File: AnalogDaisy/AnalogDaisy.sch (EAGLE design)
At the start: 21 parts, among them J1 1X2-3.5MM, J2 1X2-3.5MM, J3 1X2-3.5MM, J4 1X2-3.5MM, J5 1X2-3.5MM, J7 POWER_JACKPTH_BREAD, Q1 35A/25V/8.5mΩ, Q3 35A/25V/8.5mΩ, Q5 35A/25V/8.5mΩ, Q6 35A/25V/8.5mΩ

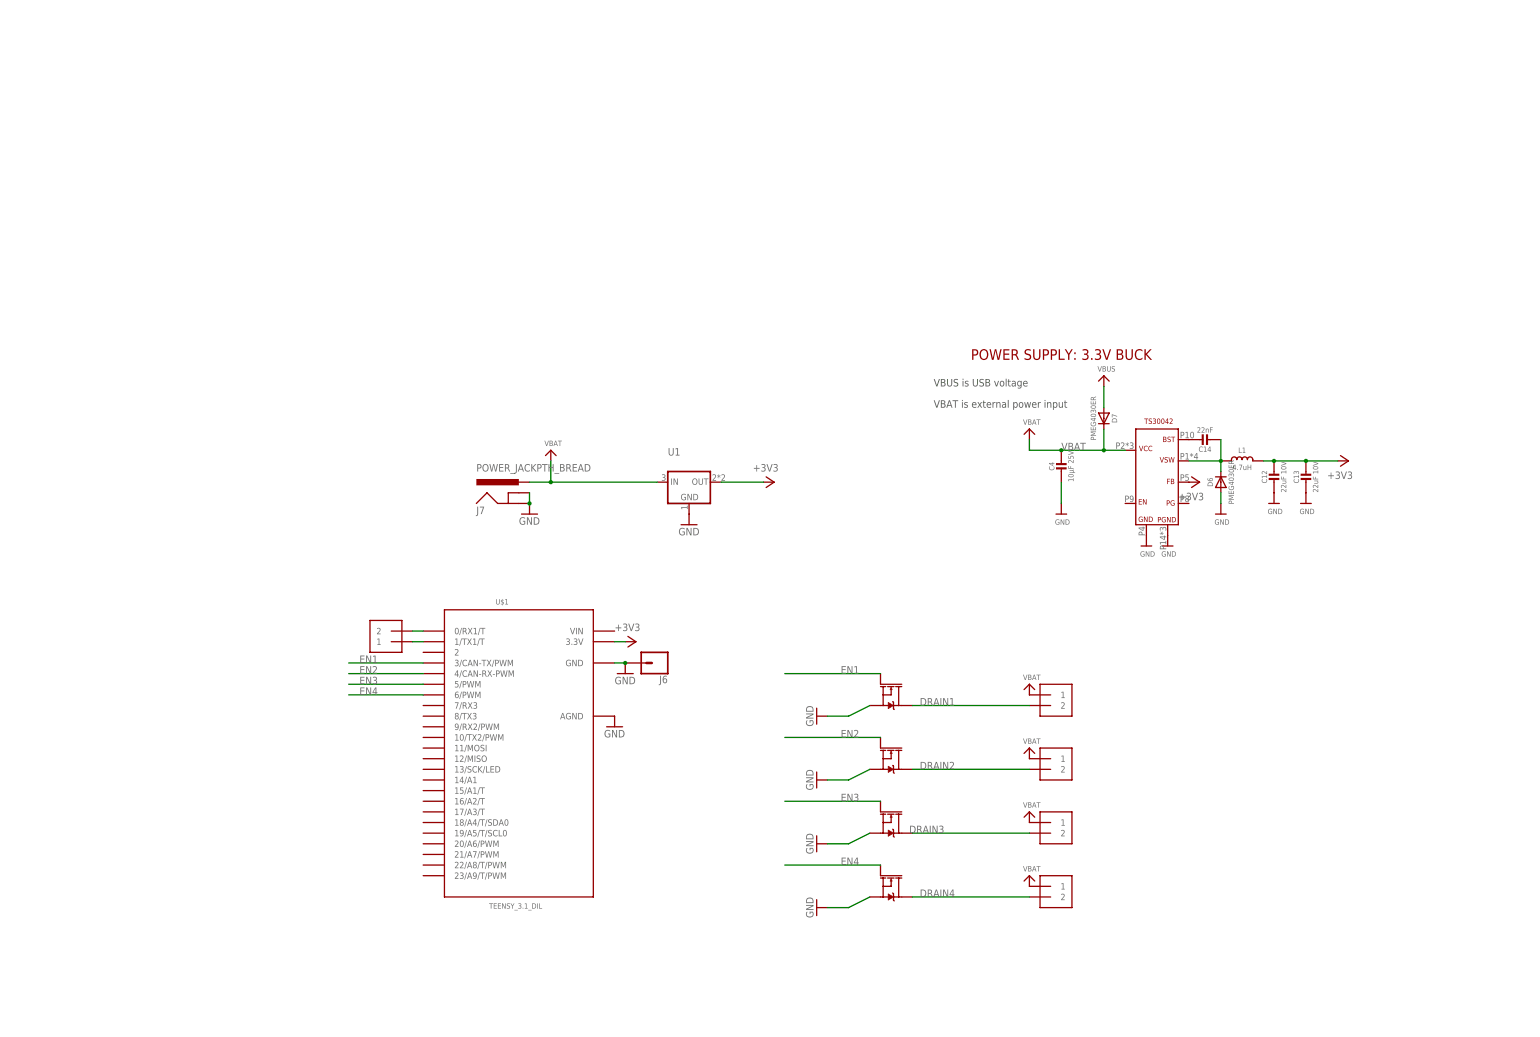
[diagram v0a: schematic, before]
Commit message: Updated AnalogDaisy
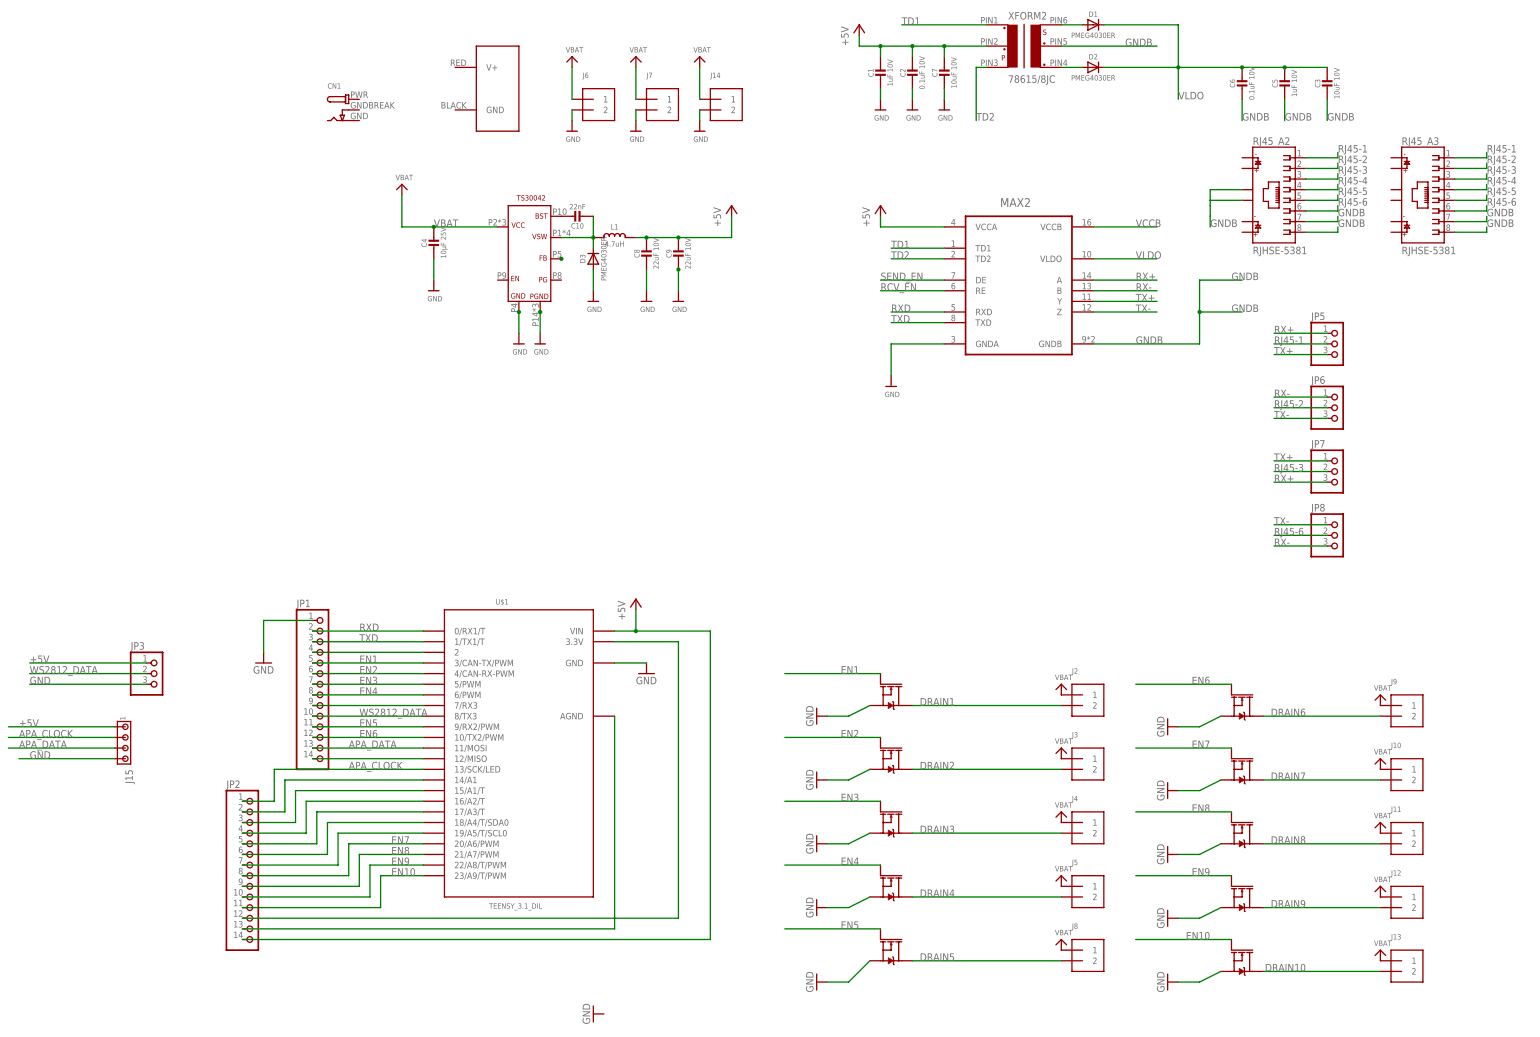
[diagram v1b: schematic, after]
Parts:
- removed C12, C13: 22uF 10V, microbuilder:CAP_CERAMIC0603MINI
- removed C14: 22nF, microbuilder:CAP_CERAMIC0603MINI
- removed D6, D7: PMEG4030ER, microbuilder:DIODESOD-123
- removed U$19: BUCK_CONVERTER, Heep:BUCK_CONVERTER
- removed U1: (no value), microbuilder:VREG_SOT223
- added C1, C5: 1uF 10V, microbuilder:CAP_CERAMIC0603MINI
- added C10: 22nF, microbuilder:CAP_CERAMIC0603MINI
- added C2, C6: 0.1uF 10V, microbuilder:CAP_CERAMIC0603MINI
- added C3, C7: 10uF 10V, microbuilder:CAP_CERAMIC0603MINI
- added C8, C9: 22uF 10V, microbuilder:CAP_CERAMIC0603MINI
- added CN1: (no value), microbuilder:DCBARRELPTH
- added D1, D2, D3: PMEG4030ER, microbuilder:DIODESOD-123
- added J10, J11, J12, J13, J14, J8, J9: (no value), microbuilder:TERMBLOCK_1X2
- added J15: (no value), My Connectors:4PIN-JST/TE
- added JP1, JP2: (no value), adafruit:PINHD-1X14
- added JP3, JP5, JP6, JP7, JP8: (no value), adafruit:PINHD-1X3
- added MAX2: MAX14853GWE+, Maxim_By_element14_Batch_1:MAX14853GWE+
- added Q10, Q2, Q4, Q7, Q8, Q9: 35A/25V/8.5mΩ, SparkFun-DiscreteSemi:MOSFET-NCH-FDD8780
- added RJ45_A2, RJ45_A3: RJHSE-5381, RJHSE-5381:RJHSE-5381
- added U$2: BUCK_CONVERTER, Heep:BUCK_CONVERTER
- added XFORM2: 78615/8JC, trafo-murata:78615/8JC
- J1: value 1X2-3.5MM -> POWERPOLE_POWER45A_DRILL; device adafruit:1X2-3.5MM -> powerpoles:POWERPOLE_POWER45A_DRILL
- J2, J3, J4, J5: value 1X2-3.5MM -> (none); device adafruit:1X2-3.5MM -> microbuilder:TERMBLOCK_1X2
- J6: device SparkFun-Connectors:CONN_01 -> microbuilder:TERMBLOCK_1X2
- J7: value POWER_JACKPTH_BREAD -> (none); device SparkFun-Connectors:POWER_JACKPTH_BREAD -> microbuilder:TERMBLOCK_1X2
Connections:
- removed net +3V3: C12.1, C13.1, L1.2, U$1.3.3V, U$19.FB, U1.OUT
- removed net VBUS: D7.A
- new net +3V1: U$2.FB
- new net +5V: C1.1, C2.1, C7.1, C9.1, J15.1, JP2.14, JP3.1, L1.2, MAX2.VCCA, U$1.VIN, XFORM2.2
- new net APA_CLOCK: J15.2, JP2.1, U$1.13/SCK/LED
- new net APA_DATA: J15.3, JP1.13, U$1.11/MOSI
- new net DRAIN10: J13.2, Q10.D
- new net DRAIN5: J8.2, Q2.D
- new net DRAIN6: J9.2, Q4.D
- new net DRAIN7: J10.2, Q7.D
- new net DRAIN8: J11.2, Q8.D
- new net DRAIN9: J12.2, Q9.D
- new net EN10: JP2.11, Q10.G, U$1.23/A9/T/PWM
- new net EN5: JP1.11, Q2.G, U$1.9/RX2/PWM
- new net EN6: JP1.12, Q4.G, U$1.10/TX2/PWM
- new net EN7: JP2.8, Q7.G, U$1.20/A6/PWM
- new net EN8: JP2.9, Q8.G, U$1.21/A7/PWM
- new net EN9: JP2.10, Q9.G, U$1.22/A8/T/PWM
- new net GNDB: C3.2, C5.2, C6.2, MAX2.GNDB, RJ45_A2.7, RJ45_A2.8, RJ45_A2.S1, RJ45_A2.S2, RJ45_A3.7, RJ45_A3.8, XFORM2.5
- new net N$10: JP1.14, U$1.12/MISO
- new net N$12: JP2.2, U$1.14/A1
- new net N$13: JP2.3, U$1.15/A1/T
- new net N$15: JP2.5, U$1.17/A3/T
- new net N$17: JP2.7, U$1.19/A5/T/SCL0
- new net N$18: JP2.13, U$1.AGND
- new net N$3: JP2.12, U$1.3.3V
- new net N$4: C10.2, D3.C, L1.1, U$2.VSW
- new net N$5: D2.A, XFORM2.4
- new net N$6: JP1.4, U$1.2
- new net N$7: JP1.9, U$1.7/RX3
- new net RCV_EN: MAX2.RE
- new net RJ45-1: JP5.2, RJ45_A2.1, RJ45_A3.1
- new net RJ45-2: JP6.2, RJ45_A2.2, RJ45_A3.2
- new net RJ45-3: JP7.2, RJ45_A2.3, RJ45_A3.3
- new net RJ45-4: RJ45_A2.4, RJ45_A3.4
- new net RJ45-5: RJ45_A2.5, RJ45_A3.5
- new net RJ45-6: JP8.2, RJ45_A2.6, RJ45_A3.6
- new net RX+: JP5.1, JP7.3, MAX2.A
- new net RX-: JP6.1, JP8.3, MAX2.B
- new net RXD: JP1.2, MAX2.RXD, U$1.0/RX1/T
- new net SEND_EN: MAX2.DE
- new net TD1: MAX2.TD1, XFORM2.1
- new net TD2: MAX2.TD2, XFORM2.3
- new net TX+: JP5.3, JP7.1, MAX2.Y
- new net TX-: JP6.3, JP8.1, MAX2.Z
- new net TXD: JP1.3, MAX2.TXD, U$1.1/TX1/T
- new net VCCB: MAX2.VCCB
- new net VLDO: C3.1, C5.1, C6.1, D1.C, D2.C, MAX2.VLDO
- new net WS2812_DATA: JP1.10, JP3.2, U$1.8/TX3
- net EN1: now also JP1.5
- net EN2: now also JP1.6
- net EN3: now also JP1.7
- net EN4: now also JP1.8
- net GND: now also C1.2, C2.2, C7.2, C8.2, C9.2, D3.A, J14.2, J15.4, J6.2, J7.2, JP1.1, JP3.3, MAX2.GNDA, Q10.S, Q2.S, Q4.S, Q7.S, Q8.S, Q9.S, U$2.GND, U$2.PGND; no longer C12.2, C13.2, D6.A, J6.1, J7.GND, J7.GNDBREAK, U$1.AGND, U$19.GND, U$19.PGND, U1.GND
- net N$1: now also C10.1, U$2.BST; no longer J1.1, U$1.1/TX1/T
- net N$14: now also JP2.4, U$1.16/A2/T; no longer C14.1, U$19.BST
- net N$16: now also JP2.6, U$1.18/A4/T/SDA0; no longer C14.2, D6.C, L1.1, U$19.VSW
- net N$2: now also D1.A, XFORM2.6; no longer J1.2, U$1.0/RX1/T
- net VBAT: now also J10.1, J11.1, J12.1, J13.1, J8.1, J9.1, U$2.VCC; no longer D7.C, J7.PWR, U$19.VCC, U1.IN
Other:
- note removed: "POWER SUPPLY: 3.3V BUCK"
- note removed: "VBAT is external power input"
- note removed: "VBUS is USB voltage"
- moved on the sheet: C4, L1
